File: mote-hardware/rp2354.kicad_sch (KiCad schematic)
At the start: 35 parts, among them J3 Conn_01x02_Pin, J4 SM03B-SRSS-TB, J6 Conn_01x03_Pin, SW1 SW_Push, SW2 SW_Push, U1 RP2354_60QFN, U4 RP Radio Module 2, Y1 ABM8-272-T3

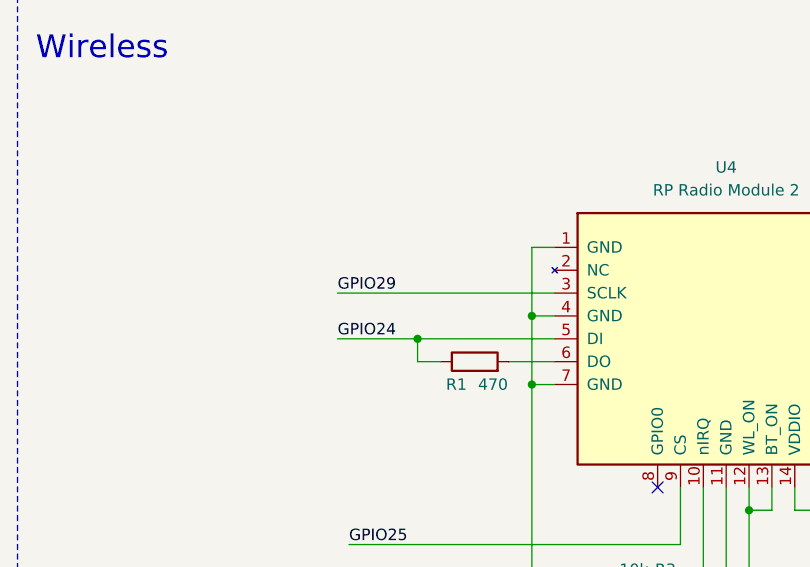
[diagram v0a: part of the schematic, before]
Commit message: Update imu schematic for SA0 -> gnd
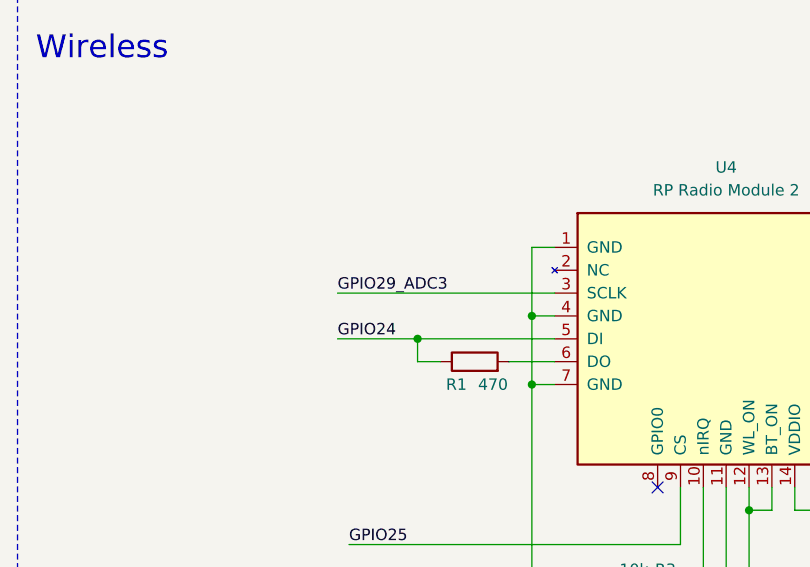
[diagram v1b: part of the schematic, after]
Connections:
- net GPIO29 is gone; now on net GPIO29_ADC3: U4.3 (SCLK)
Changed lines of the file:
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@@
 		)
 	)
-	(label "GPIO29"
+	(label "GPIO29_ADC3"
 		(at 293.37 111.76 0)
 		(effects

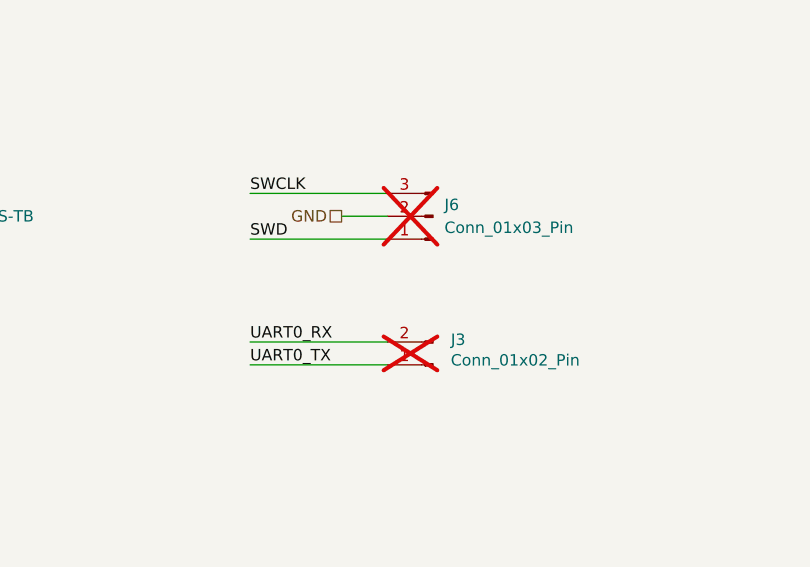
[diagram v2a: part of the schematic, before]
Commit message: GND not included in uart pins
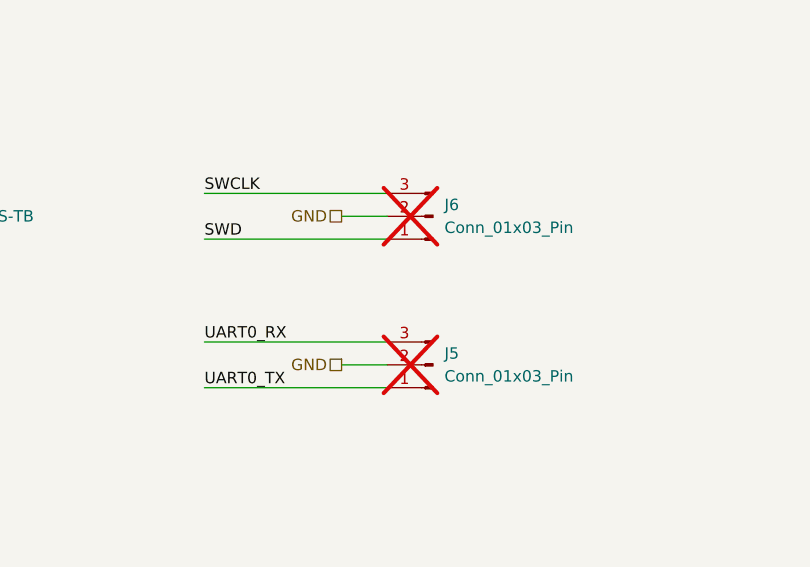
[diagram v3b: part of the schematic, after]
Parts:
- removed J3: Conn_01x02_Pin, Connector_PinHeader_2.54mm:PinHeader_1x02_P2.54mm_Vertical, symbol Connector:Conn_01x02_Pin
- added J5: Conn_01x03_Pin, Connector_PinHeader_2.54mm:PinHeader_1x03_P2.54mm_Vertical, symbol Connector:Conn_01x03_Pin
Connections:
- net GND: now also J5.2 (Pin_2)
- net UART0_RX: now also J5.3 (Pin_3)
- net UART0_TX: now also J5.1 (Pin_1)
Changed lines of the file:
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@@
 	(wire
 		(pts
-			(xy 335.28 217.17) (xy 350.52 217.17)
+			(xy 330.2 217.17) (xy 350.52 217.17)
 		)
 		(stroke
@@
 	(wire
 		(pts
+			(xy 345.44 231.14) (xy 350.52 231.14)
+		)
+		(stroke
+			(width 0)
+			(type default)
+		)
+	)
+	(wire
+		(pts
 			(xy 223.52 44.45) (xy 223.52 46.99)
 		)
@@
 	(wire
 		(pts
-			(xy 350.52 231.14) (xy 335.28 231.14)
+			(xy 350.52 233.68) (xy 330.2 233.68)
 		)
 		(stroke
@@
 	(wire
 		(pts
-			(xy 335.28 212.09) (xy 350.52 212.09)
+			(xy 330.2 212.09) (xy 350.52 212.09)
 		)
 		(stroke
@@
 	(wire
 		(pts
-			(xy 350.52 228.6) (xy 335.28 228.6)
+			(xy 350.52 228.6) (xy 330.2 228.6)
 		)
 		(stroke
@@
 	)
 	(label "UART0_RX"
-		(at 335.28 228.6 0)
+		(at 330.2 228.6 0)
 		(effects
 			(font
@@
 	)
 	(label "SWD"
-		(at 335.28 217.17 0)
+		(at 330.2 217.17 0)
 		(effects
 			(font
@@
 	)
 	(label "UART0_TX"
-		(at 335.28 231.14 0)
+		(at 330.2 233.68 0)
 		(effects
 			(font
@@
 	)
 	(label "SWCLK"
-		(at 335.28 212.09 0)
+		(at 330.2 212.09 0)
 		(effects
 			(font
@@
 		)
 	)
+	(hierarchical_label "GND"
+		(shape passive)
+		(at 345.44 231.14 180)
+		(effects
+			(font
+				(size 1.27 1.27)
+			)
+			(justify right)
+		)
+	)
 	(hierarchical_label "lidar_tx"
 		(shape output)
@@
 	)
 	(symbol
+		(lib_id "Connector:Conn_01x03_Pin")
+		(at 355.6 231.14 180)
+		(unit 1)
+		(exclude_from_sim no)
+		(in_bom no)
+		(on_board yes)
+		(dnp yes)
+		(fields_autoplaced yes)
+		(property "Reference" "J5"
+			(at 356.87 229.8699 0)
+			(effects
+				(font
+					(size 1.27 1.27)
+				)
+				(justify right)
+			)
+		)
+		(property "Value" "Conn_01x03_Pin"
+			(at 356.87 232.4099 0)
+			(effects
+				(font
+					(size 1.27 1.27)
+				)
+				(justify right)
+			)
+		)
+		(property "Footprint" "Connector_PinHeader_2.54mm:PinHeader_1x03_P2.54mm_Vertical"
+			(at 355.6 231.14 0)
+			(effects
+				(font
+					(size 1.27 1.27)
+				)
+				(hide yes)
+			)
+		)
+		(property "Datasheet" "~"
+			(at 355.6 231.14 0)
+			(effects
+				(font
+					(size 1.27 1.27)
+				)
+				(hide yes)
+			)
+		)
+		(property "Description" "Generic connector, single row, 01x03, script generated"
+			(at 355.6 231.14 0)
+			(effects
+				(font
+					(size 1.27 1.27)
+				)
+				(hide yes)
+			)
+		)
+		(property "JLCPCB_CORRECTION" ""
+			(at 355.6 231.14 0)
+			(effects
+				(font
+					(size 1.27 1.27)
+				)
+				(hide yes)
+			)
+		)
+		(pin "2"
+		)
+		(pin "3"
+		)
+		(pin "1"
+		)
+		(instances
+			(project "mote-hardware"
+				(path "/94683f5c-9cd9-448e-be96-9792537b5cb8/8aa6d869-37ab-4fd7-8af1-9416ab877c54"
+					(reference "J5")
+					(unit 1)
+				)
+			)
+		)
+	)
+	(symbol
 		(lib_id "Device:C")
 		(at 39.37 82.55 0)
@@
 					(unit 1)
 				)
-			)
-		)
-	)
-	(symbol
-		(lib_id "Connector:Conn_01x02_Pin")
-		(at 355.6 231.14 180)
-		(unit 1)
-		(exclude_from_sim no)
-		(in_bom no)
-		(on_board yes)
-		(dnp yes)
-		(property "Reference" "J3"
-			(at 358.394 228.346 0)
-			(effects
-				(font
-					(size 1.27 1.27)
-				)
-			)
-		)
-		(property "Value" "Conn_01x02_Pin"
-			(at 364.744 230.632 0)
-			(effects
-				(font
-					(size 1.27 1.27)
-				)
-			)
-		)
-		(property "Footprint" "Connector_PinHeader_2.54mm:PinHeader_1x02_P2.54mm_Vertical"
-			(at 355.6 231.14 0)
-			(effects
-				(font
-					(size 1.27 1.27)
-				)
-				(hide yes)
-			)
-		)
-		(property "Datasheet" "~"
-			(at 355.6 231.14 0)
-			(effects
-				(font
-					(size 1.27 1.27)
-				)
-				(hide yes)
-			)
-		)
-		(property "Description" "Generic connector, single row, 01x02, script generated"
-			(at 355.6 231.14 0)
-			(effects
-				(font
-					(size 1.27 1.27)
-				)
-				(hide yes)
-			)
-		)
-		(property "JLCPCB_CORRECTION" ""
-			(at 355.6 231.14 0)
-			(effects
-				(font
-					(size 1.27 1.27)
-				)
-				(hide yes)
-			)
-		)
-		(pin "1"
-		)
-		(pin "2"
-		)
-		(instances
-			(project "mote-hardware"
-				(path "/94683f5c-9cd9-448e-be96-9792537b5cb8/8aa6d869-37ab-4fd7-8af1-9416ab877c54"
-					(reference "J3")
-					(unit 1)
-				)

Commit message: Update part number for JST connector
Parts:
- J4: LCSC C160403 -> C160389
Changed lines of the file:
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@@
 			)
 		)
-		(property "LCSC" "C160403"
+		(property "LCSC" "C160389"
 			(at 294.64 213.36 0)
 			(effects

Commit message: Add rp radio module 2 PN to BOM, mark for placement
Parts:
- U4: LCSC (none) -> C49302697; now in the parts list
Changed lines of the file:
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@@
 		(unit 1)
 		(exclude_from_sim no)
-		(in_bom no)
+		(in_bom yes)
 		(on_board yes)
 		(dnp no)
@@
 			(at 336.55 116.84 0)
 			(effects
+				(font
+					(size 1.27 1.27)
+				)
+				(hide yes)
+			)
+		)
+		(property "LCSC" "C49302697"
+			(at 336.55 116.84 0)
+			(effects

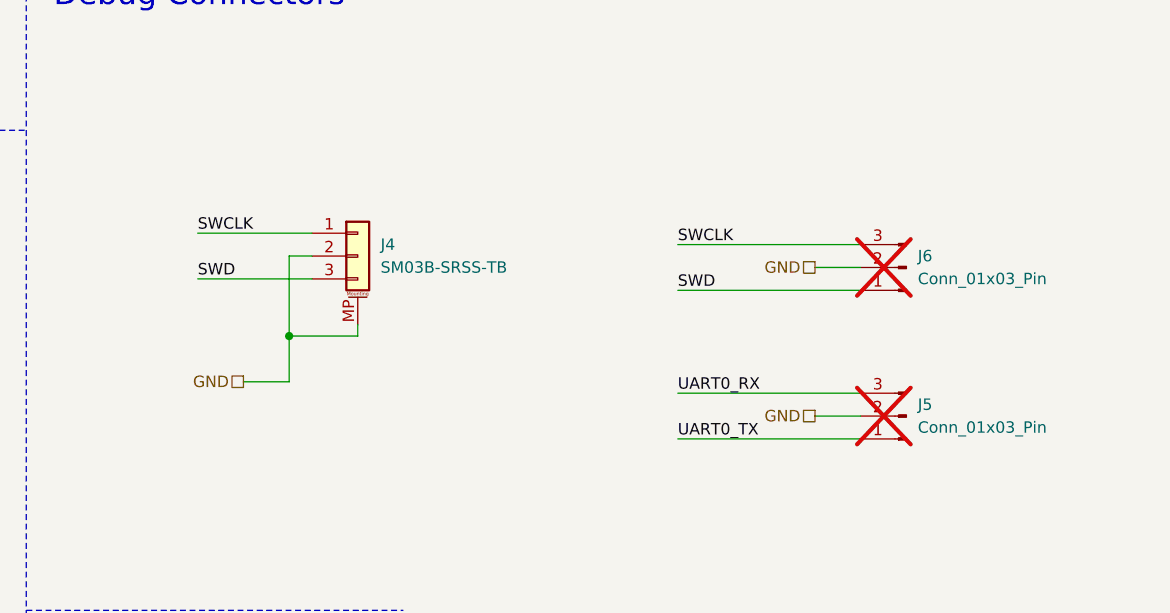
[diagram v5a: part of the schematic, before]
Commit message: Add comments to schematic, respect ground pin on SWD and UART connectors
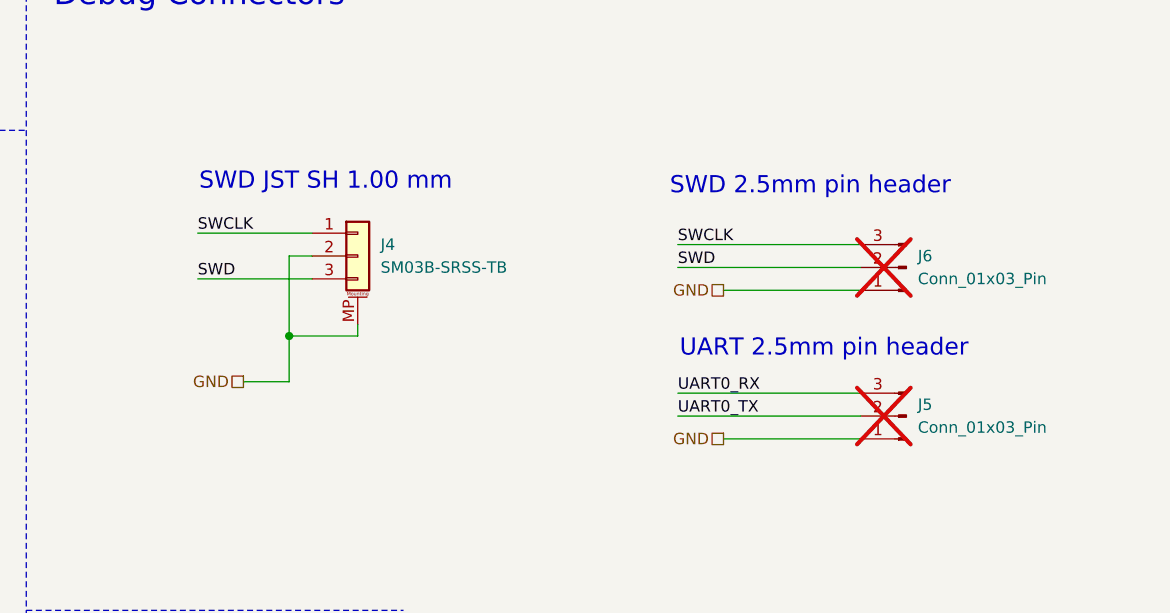
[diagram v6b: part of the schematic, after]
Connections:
- net GND: now also J5.1 (Pin_1), J6.1 (Pin_1); no longer J5.2 (Pin_2), J6.2 (Pin_2)
- net SWD: now also J6.2 (Pin_2); no longer J6.1 (Pin_1)
- net UART0_TX: now also J5.2 (Pin_2); no longer J5.1 (Pin_1)
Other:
- note added: "SWD 2.5mm pin header"
- note added: "SWD JST SH 1.00 mm"
- note added: "UART 2.5mm pin header"
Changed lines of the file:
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@@
 		)
 	)
+	(text "SWD JST SH 1.00 mm"
+		(exclude_from_sim no)
+		(at 291.084 206.248 0)
+		(effects
+			(font
+				(size 1.905 1.905)
+			)
+			(justify bottom)
+		)
+	)
 	(text "USB"
 		(exclude_from_sim no)
@@
 		)
 	)
+	(text "SWD 2.5mm pin header"
+		(exclude_from_sim no)
+		(at 344.932 206.756 0)
+		(effects
+			(font
+				(size 1.905 1.905)
+			)
+			(justify bottom)
+		)
+	)
 	(text "IMU"
 		(exclude_from_sim no)
@@
 		)
 	)
+	(text "UART 2.5mm pin header"
+		(exclude_from_sim no)
+		(at 346.456 224.79 0)
+		(effects
+			(font
+				(size 1.905 1.905)
+			)
+			(justify bottom)
+		)
+	)
 	(text "Wireless"
 		(exclude_from_sim no)
@@
 	(wire
 		(pts
-			(xy 161.29 121.92) (xy 176.53 121.92)
+			(xy 330.2 214.63) (xy 350.52 214.63)
 		)
 		(stroke
@@
 	(wire
 		(pts
-			(xy 77.47 69.85) (xy 77.47 82.55)
+			(xy 161.29 121.92) (xy 176.53 121.92)
 		)
 		(stroke
@@
 	(wire
 		(pts
-			(xy 97.79 97.79) (xy 79.375 97.79)
+			(xy 77.47 69.85) (xy 77.47 82.55)
 		)
 		(stroke
@@
 	(wire
 		(pts
-			(xy 212.09 44.45) (xy 212.09 46.99)
+			(xy 97.79 97.79) (xy 79.375 97.79)
 		)
 		(stroke
@@
 	(wire
 		(pts
-			(xy 86.36 36.83) (xy 86.36 35.56)
+			(xy 212.09 44.45) (xy 212.09 46.99)
 		)
 		(stroke
@@
 	(wire
 		(pts
-			(xy 161.29 154.94) (xy 176.53 154.94)
+			(xy 86.36 36.83) (xy 86.36 35.56)
 		)
 		(stroke
@@
 	(wire
 		(pts
-			(xy 39.37 69.85) (xy 77.47 69.85)
+			(xy 161.29 154.94) (xy 176.53 154.94)
 		)
 		(stroke
@@
 	(wire
 		(pts
-			(xy 39.37 64.77) (xy 39.37 69.85)
+			(xy 39.37 69.85) (xy 77.47 69.85)
 		)
 		(stroke
@@
 	(wire
 		(pts
-			(xy 330.2 217.17) (xy 350.52 217.17)
+			(xy 39.37 64.77) (xy 39.37 69.85)
 		)
 		(stroke
@@
 	(wire
 		(pts
-			(xy 345.44 231.14) (xy 350.52 231.14)
-		)
-		(stroke
-			(width 0)
-			(type default)
-		)
-	)
-	(wire
-		(pts
 			(xy 223.52 44.45) (xy 223.52 46.99)
 		)
@@
 		)
 	)
-	(wire
-		(pts
-			(xy 350.52 233.68) (xy 330.2 233.68)
-		)
-		(stroke
-			(width 0)
-			(type default)
-		)
-	)
 	(polyline
 		(pts
@@
 	(wire
 		(pts
+			(xy 335.28 233.68) (xy 350.52 233.68)
+		)
+		(stroke
+			(width 0)
+			(type default)
+		)
+	)
+	(wire
+		(pts
 			(xy 99.06 229.87) (xy 110.49 229.87)
 		)
@@
 	(wire
 		(pts
+			(xy 335.28 217.17) (xy 350.52 217.17)
+		)
+		(stroke
+			(width 0)
+			(type default)
+		)
+	)
+	(wire
+		(pts
 			(xy 83.82 101.6) (xy 97.79 101.6)
 		)
@@
 	(wire
 		(pts
-			(xy 345.44 214.63) (xy 350.52 214.63)
-		)
-		(stroke
-			(width 0)
-			(type default)
-		)
-	)
-	(wire
-		(pts
 			(xy 344.17 135.89) (xy 359.41 135.89)
 		)
@@
 	(wire
 		(pts
+			(xy 350.52 231.14) (xy 330.2 231.14)
+		)
+		(stroke
+			(width 0)
+			(type default)
+		)
+	)
+	(wire
+		(pts
 			(xy 177.8 44.45) (xy 177.8 46.99)
 		)
@@
 		)
 	)
-	(label "SWD"
-		(at 330.2 217.17 0)
-		(effects
-			(font
-				(size 1.27 1.27)
-			)
-			(justify left bottom)
-		)
-	)
 	(label "+1v1"
 		(at 57.15 73.66 180)
@@
 		)
 	)
-	(label "UART0_TX"
-		(at 330.2 233.68 0)
-		(effects
-			(font
-				(size 1.27 1.27)
-			)
-			(justify left bottom)
-		)
-	)
 	(label "XOUT"
 		(at 83.82 127 0)
@@
 		)
 	)
+	(label "SWD"
+		(at 330.2 214.63 0)
+		(effects
+			(font
+				(size 1.27 1.27)
+			)
+			(justify left bottom)
+		)
+	)
 	(label "GPIO22"
 		(at 176.53 142.24 180)
@@
 		)
 	)
+	(label "UART0_TX"
+		(at 330.2 231.14 0)
+		(effects
+			(font
+				(size 1.27 1.27)
+			)
+			(justify left bottom)
+		)
+	)
 	(label "~{USB_BOOT}"
 		(at 58.42 97.79 0)
@@
 		)
 	)
+	(hierarchical_label "GND"
+		(shape passive)
+		(at 335.28 217.17 180)
+		(effects
+			(font
+				(size 1.27 1.27)
+			)
+			(justify right)
+		)
+	)
 	(hierarchical_label "CC1"
 		(shape input)
@@
 		)
 	)
-	(hierarchical_label "GND"
-		(shape passive)
-		(at 345.44 231.14 180)
-		(effects
-			(font
-				(size 1.27 1.27)
-			)
-			(justify right)
-		)
-	)
 	(hierarchical_label "lidar_tx"
 		(shape output)
@@
 		)
 	)
-	(hierarchical_label "GND"
-		(shape passive)
-		(at 345.44 214.63 180)
-		(effects
-			(font
-				(size 1.27 1.27)
-			)
-			(justify right)
-		)
-	)
 	(hierarchical_label "motor_left_encoder_b"
 		(shape output)
@@
 		)
 	)
+	(hierarchical_label "GND"
+		(shape passive)
+		(at 335.28 233.68 180)
+		(effects
+			(font
+				(size 1.27 1.27)
+			)
+			(justify right)
+		)
+	)

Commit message: Add position corrections
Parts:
- C10, C11, C12, C13, C14, C15, C16, C17, C18, C3, C4, C6, C7, C8, C9, FB1, H5, H6, J4, L1, R1, R2, R3, R4, R5, R6, R7, R8, SW1, SW2, U1, U4, Y1: JLCPCB_CORRECTION (none) -> 0; 0; 0
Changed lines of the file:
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@@
 			)
 		)
-		(property "JLCPCB_CORRECTION" ""
+		(property "JLCPCB_CORRECTION" "0; 0; 0"
 			(at 176.53 69.85 90)
 			(effects
@@
 			)
 		)
-		(property "JLCPCB_CORRECTION" ""
+		(property "JLCPCB_CORRECTION" "0; 0; 0"
 			(at 176.53 78.74 90)
 			(effects
@@
 			)
 		)
-		(property "JLCPCB_CORRECTION" ""
+		(property "JLCPCB_CORRECTION" "0; 0; 0"
 			(at 154.94 40.64 0)
 			(effects
@@
 			)
 		)
-		(property "JLCPCB_CORRECTION" ""
+		(property "JLCPCB_CORRECTION" "0; 0; 0"
 			(at 166.37 40.64 0)
 			(effects
@@
 			)
 		)
-		(property "JLCPCB_CORRECTION" ""
+		(property "JLCPCB_CORRECTION" "0; 0; 0"
 			(at 177.8 40.64 0)
 			(effects
@@
 			)
 		)
-		(property "JLCPCB_CORRECTION" ""
+		(property "JLCPCB_CORRECTION" "0; 0; 0"
 			(at 189.23 40.64 0)
 			(effects
@@
 			)
 		)
-		(property "JLCPCB_CORRECTION" ""
+		(property "JLCPCB_CORRECTION" "0; 0; 0"
 			(at 200.66 40.64 0)
 			(effects
@@
 			)
 		)
-		(property "JLCPCB_CORRECTION" ""
+		(property "JLCPCB_CORRECTION" "0; 0; 0"
 			(at 212.09 40.64 0)
 			(effects
@@
 			)
 		)
-		(property "JLCPCB_CORRECTION" ""
+		(property "JLCPCB_CORRECTION" "0; 0; 0"
 			(at 97.79 40.64 0)
 			(effects
@@
 			)
 		)
-		(property "JLCPCB_CORRECTION" ""
+		(property "JLCPCB_CORRECTION" "0; 0; 0"
 			(at 364.49 135.89 90)
 			(effects
@@
 			)
 		)
-		(property "JLCPCB_CORRECTION" ""
+		(property "JLCPCB_CORRECTION" "0; 0; 0"
 			(at 52.07 139.7 90)
 			(effects
@@
 			)
 		)
-		(property "JLCPCB_CORRECTION" ""
+		(property "JLCPCB_CORRECTION" "0; 0; 0"
 			(at 265.43 264.16 0)
 			(effects
@@
 			)
 		)
-		(property "JLCPCB_CORRECTION" ""
+		(property "JLCPCB_CORRECTION" "0; 0; 0"
 			(at 129.54 119.38 0)
 			(effects
@@
 			)
 		)
-		(property "JLCPCB_CORRECTION" ""
+		(property "JLCPCB_CORRECTION" "0; 0; 0"
 			(at 223.52 40.64 0)
 			(effects
@@
 			)
 		)
-		(property "JLCPCB_CORRECTION" ""
+		(property "JLCPCB_CORRECTION" "0; 0; 0"
 			(at 64.77 139.7 0)
 			(effects
@@
 			)
 		)
-		(property "JLCPCB_CORRECTION" ""
+		(property "JLCPCB_CORRECTION" "0; 0; 0"
 			(at 75.565 97.79 90)
 			(effects
@@
 			)
 		)
-		(property "JLCPCB_CORRECTION" ""
+		(property "JLCPCB_CORRECTION" "0; 0; 0"
 			(at 73.66 64.77 0)
 			(effects
@@
 			)
 		)
-		(property "JLCPCB_CORRECTION" ""
+		(property "JLCPCB_CORRECTION" "0; 0; 0"
 			(at 39.37 82.55 0)
 			(effects
@@
 			)
 		)
-		(property "JLCPCB_CORRECTION" ""
+		(property "JLCPCB_CORRECTION" "0; 0; 0"
 			(at 275.59 271.78 0)
 			(effects
@@
 			)
 		)
-		(property "JLCPCB_CORRECTION" ""
+		(property "JLCPCB_CORRECTION" "0; 0; 0"
 			(at 313.69 48.26 0)
 			(effects
@@
 			)
 		)
-		(property "JLCPCB_CORRECTION" ""
+		(property "JLCPCB_CORRECTION" "0; 0; 0"
 			(at 50.8 82.55 0)
 			(effects
@@
 			)
 		)
-		(property "JLCPCB_CORRECTION" ""
+		(property "JLCPCB_CORRECTION" "0; 0; 0"
 			(at 85.09 69.85 0)
 			(effects
@@
 			)
 		)
-		(property "JLCPCB_CORRECTION" ""
+		(property "JLCPCB_CORRECTION" "0; 0; 0"
 			(at 294.64 213.36 0)
 			(effects
@@
 			)
 		)
-		(property "JLCPCB_CORRECTION" ""
+		(property "JLCPCB_CORRECTION" "0; 0; 0"
 			(at 346.71 48.26 90)
 			(effects
@@
 			)
 		)
-		(property "JLCPCB_CORRECTION" ""
+		(property "JLCPCB_CORRECTION" "0; 0; 0"
 			(at 74.93 40.64 0)
 			(effects
@@
 			)
 		)
-		(property "JLCPCB_CORRECTION" ""
+		(property "JLCPCB_CORRECTION" "0; 0; 0"
 			(at 58.42 105.41 90)
 			(effects
@@
 			)
 		)
-		(property "JLCPCB_CORRECTION" ""
+		(property "JLCPCB_CORRECTION" "0; 0; 0"
 			(at 86.36 40.64 0)
 			(effects
@@
 			)
 		)
-		(property "JLCPCB_CORRECTION" ""
+		(property "JLCPCB_CORRECTION" "0; 0; 0"
 			(at 327.66 144.78 90)
 			(effects
@@
 			)
 		)
-		(property "JLCPCB_CORRECTION" ""
+		(property "JLCPCB_CORRECTION" "0; 0; 0"
 			(at 336.55 116.84 0)
 			(effects
@@
 			)
 		)
-		(property "JLCPCB_CORRECTION" ""
+		(property "JLCPCB_CORRECTION" "0; 0; 0"
 			(at 66.04 82.55 0)
 			(effects
@@
 			)
 		)
-		(property "JLCPCB_CORRECTION" ""
+		(property "JLCPCB_CORRECTION" "0; 0; 0"
 			(at 328.93 43.18 90)
 			(effects
@@
 			)
 		)
-		(property "JLCPCB_CORRECTION" ""
+		(property "JLCPCB_CORRECTION" "0; 0; 0"
 			(at 308.61 119.38 90)
 			(effects
@@
 			)
 		)
-		(property "JLCPCB_CORRECTION" ""
+		(property "JLCPCB_CORRECTION" "0; 0; 0"
 			(at 313.69 38.1 0)
 			(effects

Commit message: Update offsets
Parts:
- J4, L1: JLCPCB_CORRECTION 0; 0; 0 -> 0; 0; 180
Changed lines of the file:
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@@
 			)
 		)
-		(property "JLCPCB_CORRECTION" "0; 0; 0"
+		(property "JLCPCB_CORRECTION" "0; 0; 180"
 			(at 294.64 213.36 0)
 			(effects
@@
 			)
 		)
-		(property "JLCPCB_CORRECTION" "0; 0; 0"
+		(property "JLCPCB_CORRECTION" "0; 0; 180"
 			(at 66.04 82.55 0)
 			(effects
